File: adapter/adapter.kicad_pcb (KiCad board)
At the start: 2 copper layers, 93.5 x 73.2 mm, 38 parts, among them J10 Ribbon, J11 Ribbon, J12 Ribbon, J9 Ribbon, Q1 Q_NMOS_GSD, Q2 Q_NMOS_GSD, Q3 Q_NMOS_GSD, Q4 Q_NMOS_GSD, SW1 SW_SPST, SW2 SW_SPST, SW3 SW_SPDT, SW4 SW_SPDT, U1 xiao-ble, U2 xiao-ble, U3 AP9101CK6, U4 AP9101CK6

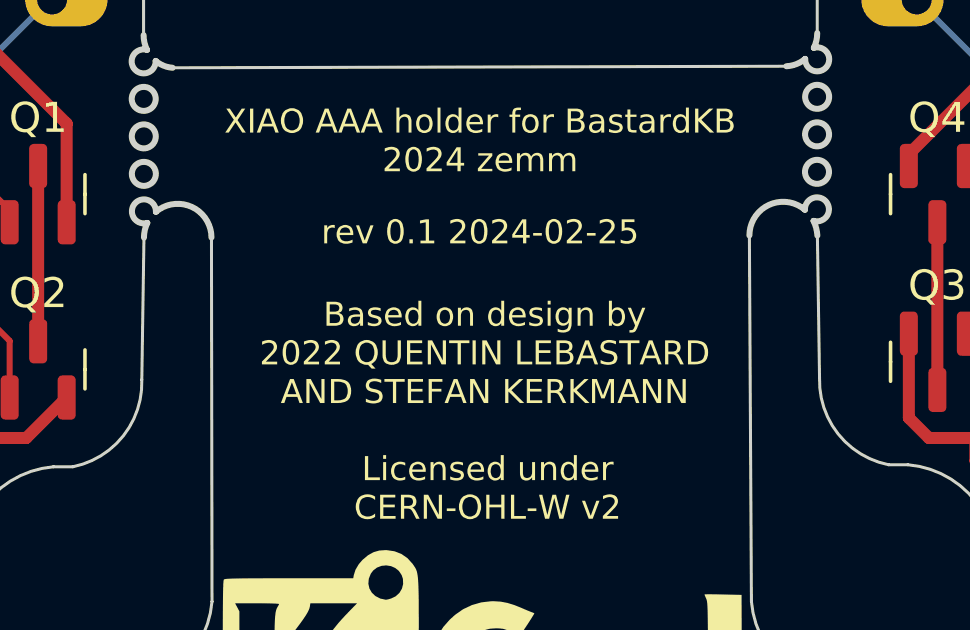
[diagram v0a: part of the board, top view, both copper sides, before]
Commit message: Docs: Make derivative work more explicit in the pcb text
The previous version of the text in the PCB could have been misinterpreted so that the design of this PCB is by the creators of the original, which is not the case. This is an unnofficial derivative work. Trying to make it more obvious.
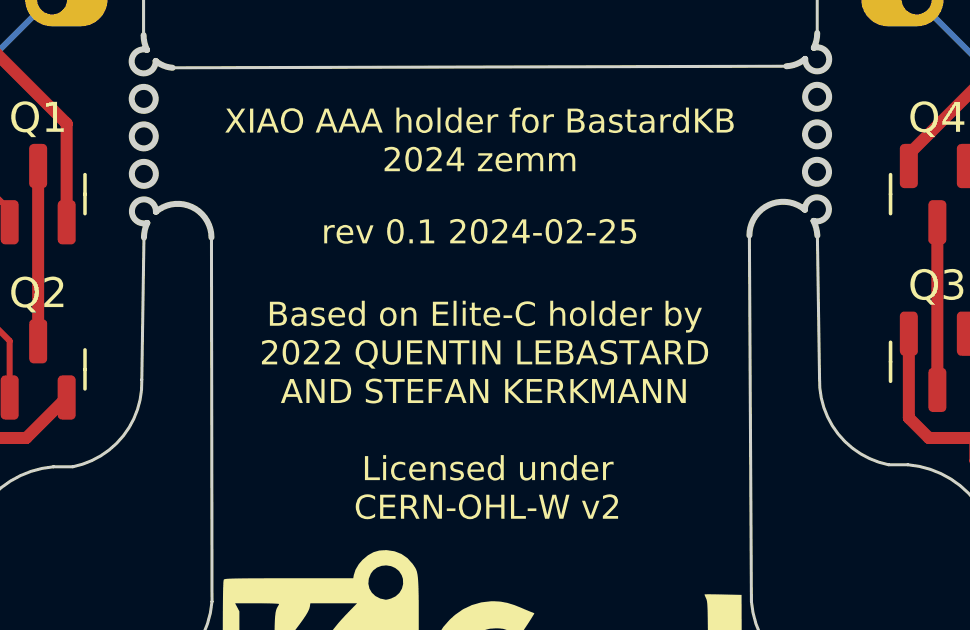
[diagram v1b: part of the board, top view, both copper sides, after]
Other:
- board text added: "Based on Elite-C holder by 2022 QUENTIN LEBASTARD AND STEFAN KERKMANN"
- board text removed: "Based on design by 2022 QUENTIN LEBASTARD AND STEFAN KERKMANN"
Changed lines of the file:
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@@
     (effects (font (size 0.8 0.8) (thickness 0.15)) (justify mirror))
   )
-  (gr_text "Based on design by\n2022 QUENTIN LEBASTARD\nAND STEFAN KERKMANN\n" (at 155.448 96.266) (layer "B.SilkS")
+  (gr_text "Based on Elite-C holder by\n2022 QUENTIN LEBASTARD\nAND STEFAN KERKMANN\n" (at 155.448 96.266) (layer "B.SilkS")
     (effects (font (size 0.8 0.8) (thickness 0.15)) (justify mirror))
   )
@@
     (effects (font (size 0.8 0.8) (thickness 0.15)))
   )
-  (gr_text "Based on design by\n2022 QUENTIN LEBASTARD\nAND STEFAN KERKMANN" (at 155.602994 96.236539) (layer "F.SilkS")
+  (gr_text "Based on Elite-C holder by\n2022 QUENTIN LEBASTARD\nAND STEFAN KERKMANN" (at 155.602994 96.236539) (layer "F.SilkS")
     (effects (font (size 0.8 0.8) (thickness 0.15)))
   )
